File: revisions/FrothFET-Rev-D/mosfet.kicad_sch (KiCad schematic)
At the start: 23 parts, among them J1 Conn_01x01, Q1 BSC010N04LS, U2 LTC7004EMSE-PBF, U3 ACS725xLCTR-20AU

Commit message: tweaks to rev d
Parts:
- C66, R71: now left out of the parts list
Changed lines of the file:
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@@
 		(unit 1)
 		(exclude_from_sim no)
-		(in_bom yes)
+		(in_bom no)
 		(on_board yes)
 		(dnp yes)
@@
 		(unit 1)
 		(exclude_from_sim no)
-		(in_bom yes)
+		(in_bom no)
 		(on_board yes)
 		(dnp yes)

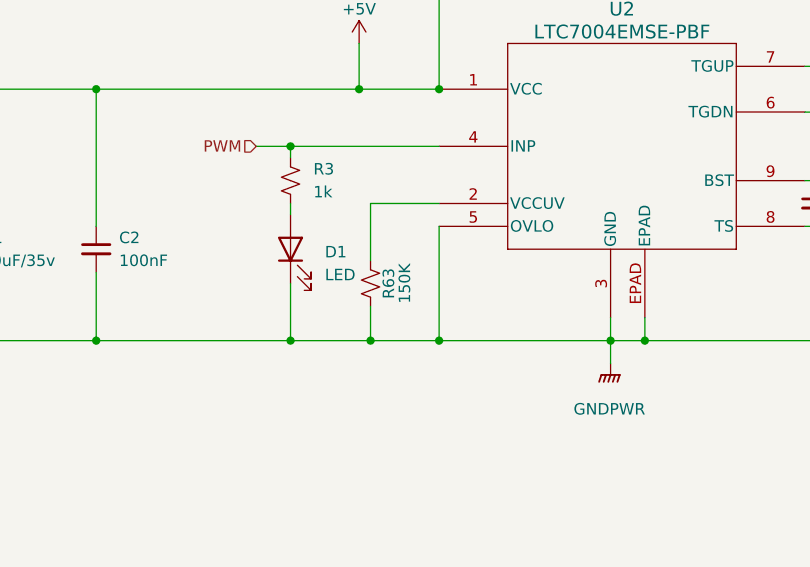
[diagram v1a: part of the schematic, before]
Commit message: removed uvlo resistor, tied to gnd.
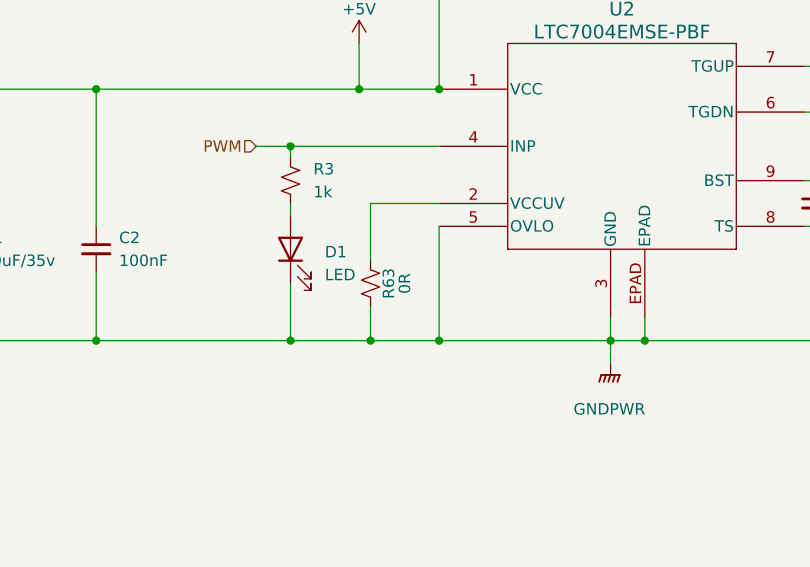
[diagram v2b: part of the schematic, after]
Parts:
- R63: value 150K -> 0R
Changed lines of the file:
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@@
 			)
 		)
-		(property "Value" "150K"
+		(property "Value" "0R"
 			(at 74.93 80.01 90)
 			(effects
